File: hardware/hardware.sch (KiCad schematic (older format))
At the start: 23 parts, among them J1 6P6C, J2 RJ45_LED_Shielded, Q1 BUK7M33-60EX, U1 Teensy4.1_DEV-16771, U2 LT1910, U3 OKI, U4 OKI-78SR-3.3_1.5-W36H-C

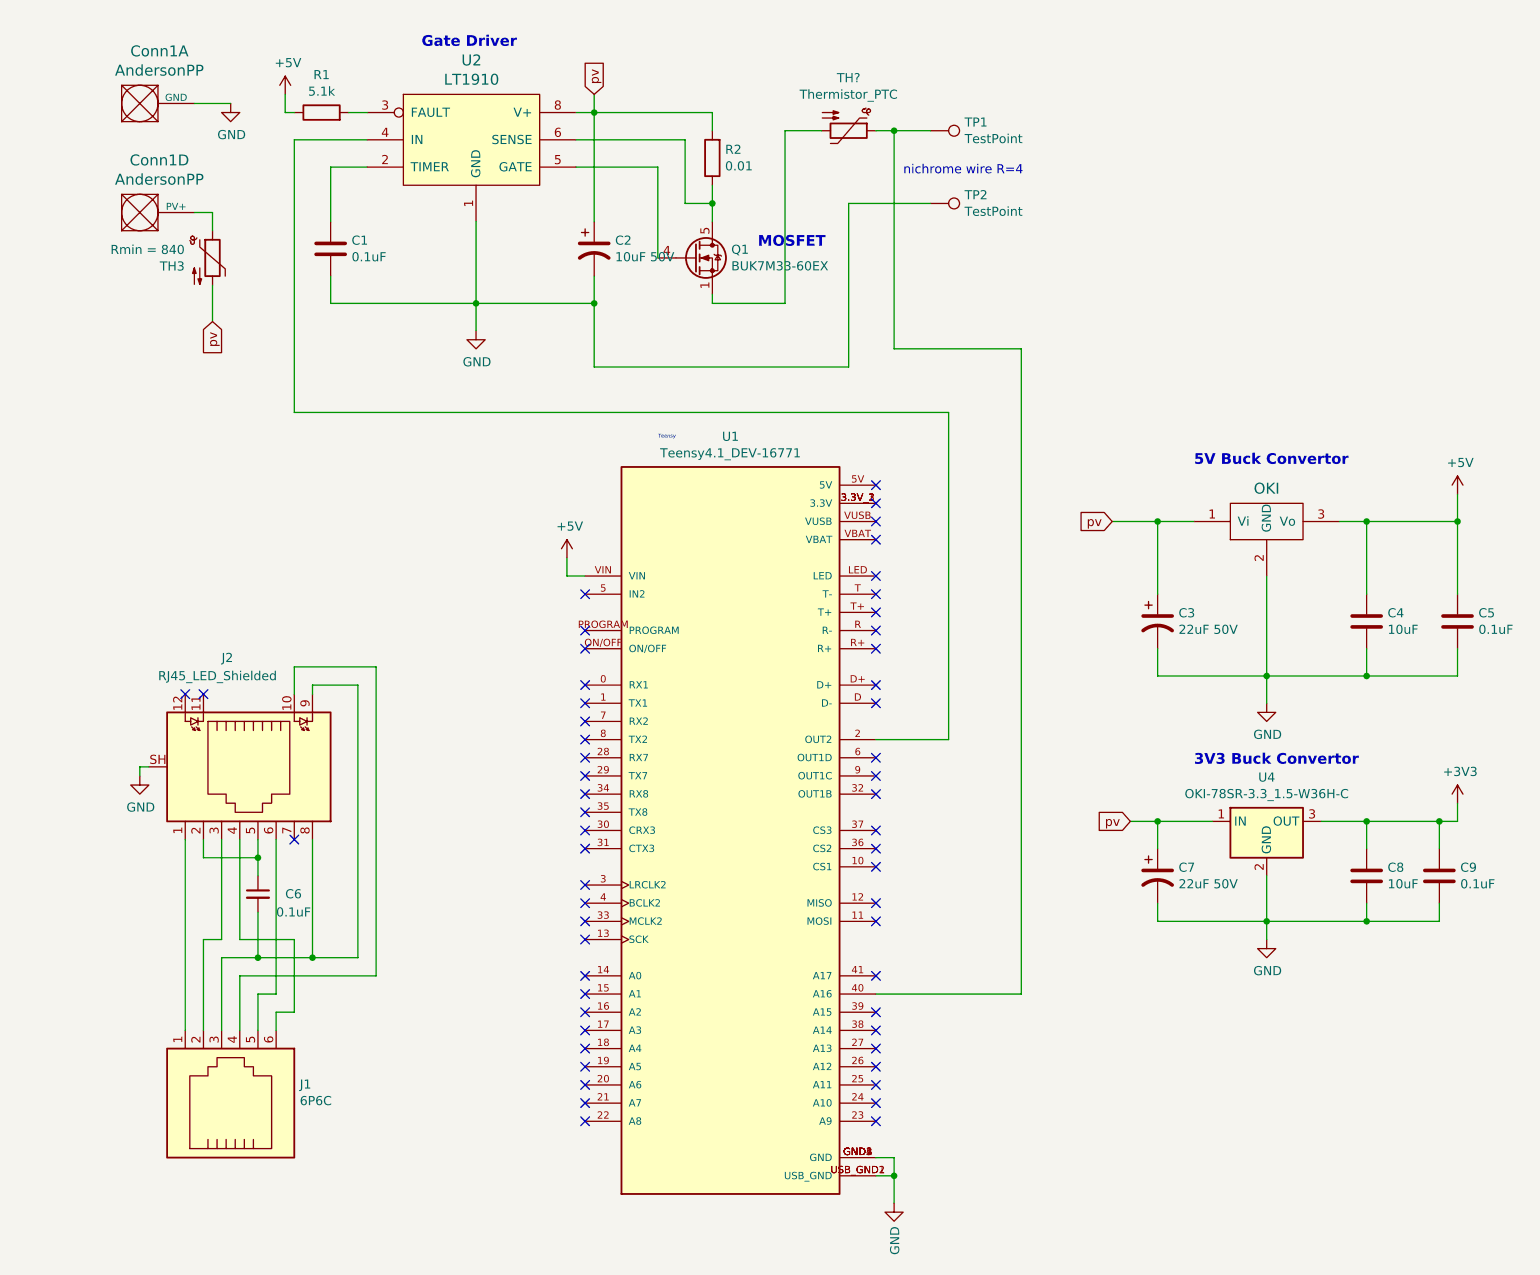
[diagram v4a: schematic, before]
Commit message: Notated and reorganized schematic
Removed measurement resistor in gate driver circuit, removed thermistor to replace with a different sensor, and wrote a note on the Andersons
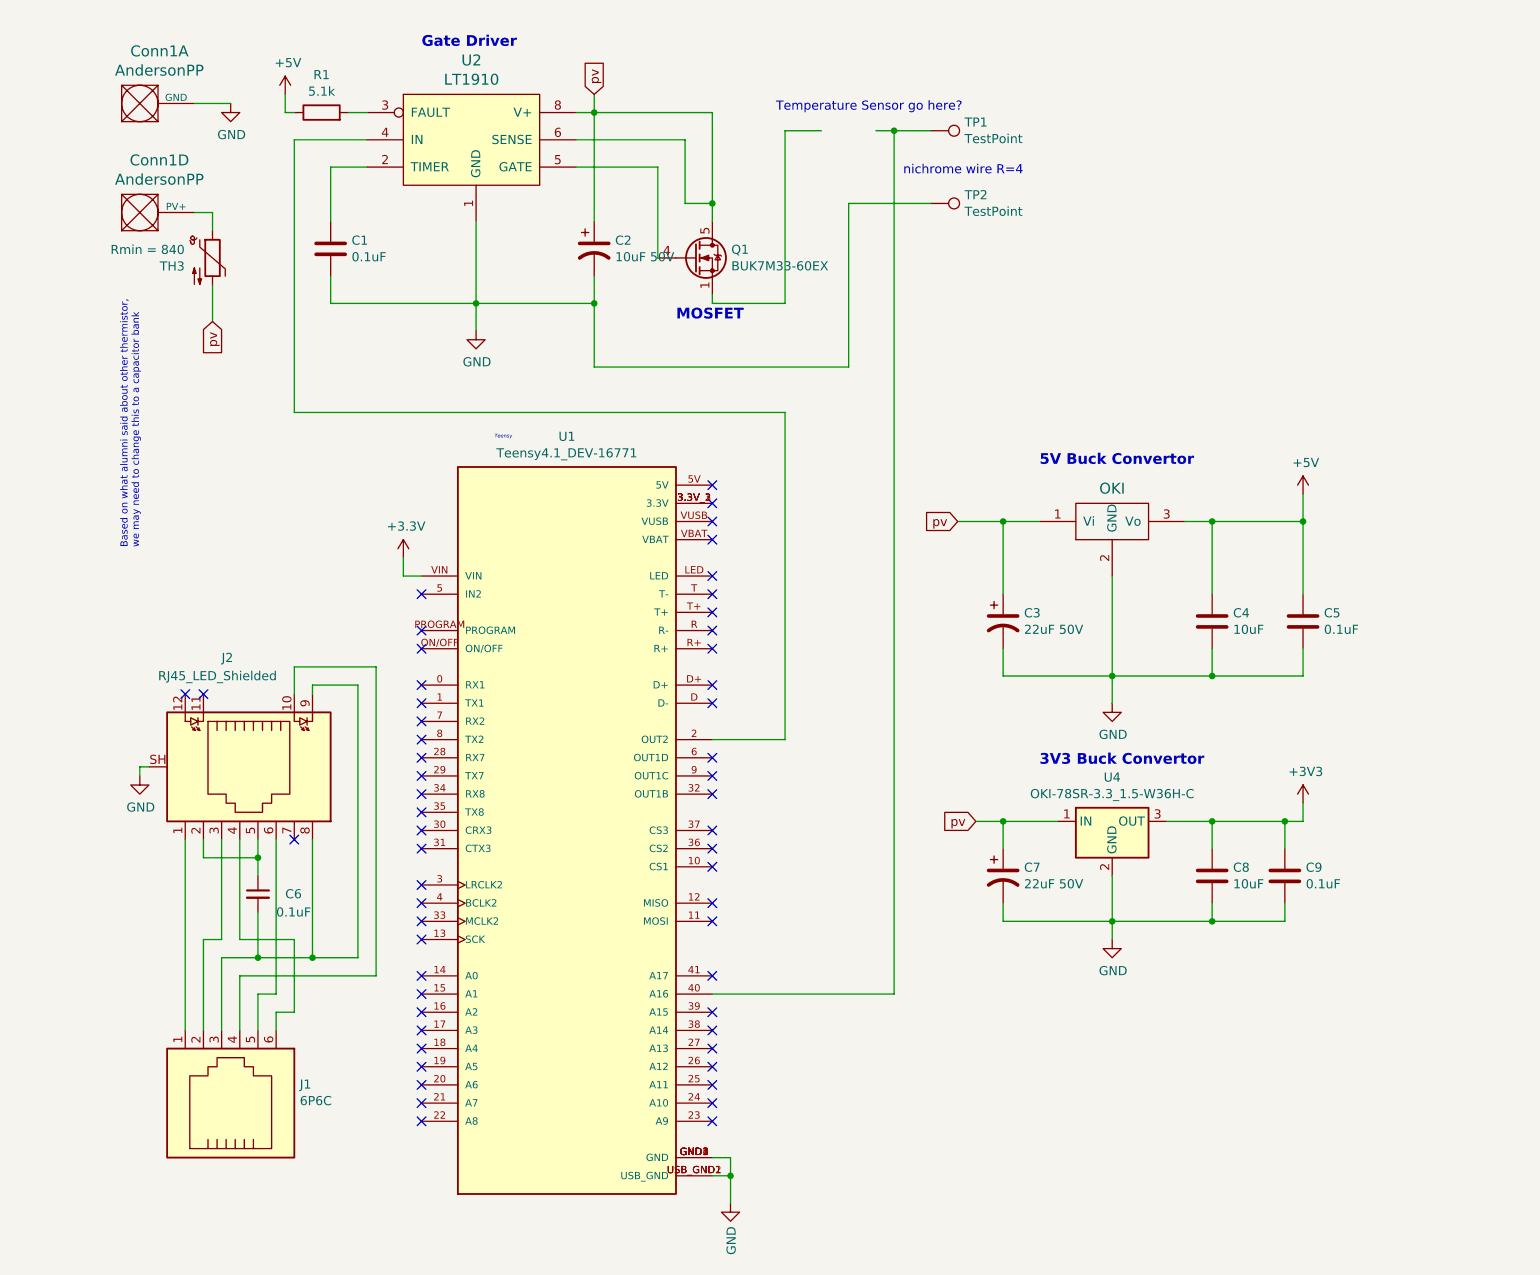
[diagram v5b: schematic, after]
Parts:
- removed R2: 0.01, symbol Device:R
- removed TH?: Thermistor_PTC, symbol Device:Thermistor_PTC
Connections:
- net +3V3: now also U1.VIN
- net +5V: no longer U1.VIN
- net pv: now also Q1.5 (D), U2.6 (SENSE)
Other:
- note added: "Based on what alumni said about other thermistor, \nwe may need to change this to a capacitor bank"
- note added: "Temperature Sensor go here?"
- moved on the sheet: C3, C4, C5, C7, C8, C9, U1, U4

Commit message: Applied footprints to capacitors
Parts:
- C1, C2, C3, C4, C5, C6, C7, C8, C9: footprint (none) -> Capacitor_SMD:C_0603_1608Metric_Pad1.08x0.95mm_HandSolder
- U1: footprint MODULE_DEV-16771 -> MRDT_Shields:MODULE_DEV-16771
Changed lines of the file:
@@
 F 0 "C1" H 1965 1746 50  0000 L CNN
 F 1 "0.1uF" H 1965 1655 50  0000 L CNN
-F 2 "" H 1888 1550 50  0001 C CNN
+F 2 "Capacitor_SMD:C_0603_1608Metric_Pad1.08x0.95mm_HandSolder" H 1888 1550 50  0001 C CNN
 F 3 "~" H 1850 1700 50  0001 C CNN
 	1    1850 1700
@@
 F 0 "C2" H 3415 1746 50  0000 L CNN
 F 1 "10uF 50V" H 3415 1655 50  0000 L CNN
-F 2 "" H 3300 1700 50  0001 C CNN
+F 2 "Capacitor_SMD:C_0603_1608Metric_Pad1.08x0.95mm_HandSolder" H 3300 1700 50  0001 C CNN
 F 3 "~" H 3300 1700 50  0001 C CNN
 	1    3300 1700
@@
 F 0 "C3" H 5665 3796 50  0000 L CNN
 F 1 "22uF 50V" H 5665 3705 50  0000 L CNN
-F 2 "" H 5550 3750 50  0001 C CNN
+F 2 "Capacitor_SMD:C_0603_1608Metric_Pad1.08x0.95mm_HandSolder" H 5550 3750 50  0001 C CNN
 F 3 "~" H 5550 3750 50  0001 C CNN
 	1    5550 3750
@@
 F 0 "C4" H 6815 3796 50  0000 L CNN
 F 1 "10uF" H 6815 3705 50  0000 L CNN
-F 2 "" H 6738 3600 50  0001 C CNN
+F 2 "Capacitor_SMD:C_0603_1608Metric_Pad1.08x0.95mm_HandSolder" H 6738 3600 50  0001 C CNN
 F 3 "~" H 6700 3750 50  0001 C CNN
 	1    6700 3750
@@
 F 0 "C5" H 7315 3796 50  0000 L CNN
 F 1 "0.1uF" H 7315 3705 50  0000 L CNN
-F 2 "" H 7238 3600 50  0001 C CNN
+F 2 "Capacitor_SMD:C_0603_1608Metric_Pad1.08x0.95mm_HandSolder" H 7238 3600 50  0001 C CNN
 F 3 "~" H 7200 3750 50  0001 C CNN
 	1    7200 3750
@@
 F 0 "C7" H 5665 5196 50  0000 L CNN
 F 1 "22uF 50V" H 5665 5105 50  0000 L CNN
-F 2 "" H 5550 5150 50  0001 C CNN
+F 2 "Capacitor_SMD:C_0603_1608Metric_Pad1.08x0.95mm_HandSolder" H 5550 5150 50  0001 C CNN
 F 3 "~" H 5550 5150 50  0001 C CNN
 	1    5550 5150
@@
 F 0 "C8" H 6815 5196 50  0000 L CNN
 F 1 "10uF" H 6815 5105 50  0000 L CNN
-F 2 "" H 6738 5000 50  0001 C CNN
+F 2 "Capacitor_SMD:C_0603_1608Metric_Pad1.08x0.95mm_HandSolder" H 6738 5000 50  0001 C CNN
 F 3 "~" H 6700 5150 50  0001 C CNN
 	1    6700 5150
@@
 F 0 "C9" H 7215 5196 50  0000 L CNN
 F 1 "0.1uF" H 7215 5105 50  0000 L CNN
-F 2 "" H 7138 5000 50  0001 C CNN
+F 2 "Capacitor_SMD:C_0603_1608Metric_Pad1.08x0.95mm_HandSolder" H 7138 5000 50  0001 C CNN
 F 3 "~" H 7100 5150 50  0001 C CNN
 	1    7100 5150
@@
 F 0 "U1" H 3150 7067 50  0000 C CNN
 F 1 "Teensy4.1_DEV-16771" H 3150 6976 50  0000 C CNN
-F 2 "MODULE_DEV-16771" H 5250 4600 50  0001 L BNN
+F 2 "MRDT_Shields:MODULE_DEV-16771" H 5250 4600 50  0001 L BNN
 F 3 "" H 3150 4900 50  0001 L BNN
 F 4 "Manufacturer recommendations" H 5250 4350 50  0001 L BNN "STANDARD"
@@
 F 0 "C6" H 1600 5250 50  0000 L CNN
 F 1 "0.1uF" H 1550 5150 50  0000 L CNN
-F 2 "" H 1450 5250 50  0001 C CNN
+F 2 "Capacitor_SMD:C_0603_1608Metric_Pad1.08x0.95mm_HandSolder" H 1450 5250 50  0001 C CNN
 F 3 "~" H 1450 5250 50  0001 C CNN
 	1    1450 5250
@@
 	3950 5800 4950 5800
 $Comp
-L power:+3.3V #PWR?
+L power:+3.3V #PWR0101
 U 1 1 617FDF47
 P 2250 3400
-F 0 "#PWR?" H 2250 3250 50  0001 C CNN
+F 0 "#PWR0101" H 2250 3250 50  0001 C CNN
 F 1 "+3.3V" H 2265 3573 50  0000 C CNN
 F 2 "" H 2250 3400 50  0001 C CNN

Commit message: Assigned footprints and started layout
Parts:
- Conn1: footprint (none) -> MRDT_Connectors:Anderson_1_Horizontal
- R1: footprint (none) -> Resistor_SMD:R_0603_1608Metric_Pad0.98x0.95mm_HandSolder
- U2: footprint (none) -> Package_SO:SOIC-8-N7_3.9x4.9mm_P1.27mm
- U3: footprint (none) -> MRDT_Devices:OKI_Horizontal
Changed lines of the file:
@@
 F 0 "Conn1" H 908 1987 60  0000 C CNN
 F 1 "AndersonPP" H 908 1881 60  0000 C CNN
-F 2 "" H 550 1050 60  0001 C CNN
+F 2 "MRDT_Connectors:Anderson_1_Horizontal" H 550 1050 60  0001 C CNN
 F 3 "" H 550 1050 60  0001 C CNN
 	4    700  1600
@@
 F 0 "Conn1" H 908 1387 60  0000 C CNN
 F 1 "AndersonPP" H 908 1281 60  0000 C CNN
-F 2 "" H 550 450 60  0001 C CNN
+F 2 "MRDT_Connectors:Anderson_1_Horizontal" H 550 450 60  0001 C CNN
 F 3 "" H 550 450 60  0001 C CNN
 	1    700  1000
@@
 F 0 "U2" H 2625 2037 60  0000 C CNN
 F 1 "LT1910" H 2625 1931 60  0000 C CNN
-F 2 "" H 2250 1350 60  0001 C CNN
+F 2 "Package_SO:SOIC-8-N7_3.9x4.9mm_P1.27mm" H 2250 1350 60  0001 C CNN
 F 3 "" H 2250 1350 60  0001 C CNN
 	1    2250 1350
@@
 F 0 "R1" V 2007 950 50  0000 C CNN
 F 1 "5.1k" V 1916 950 50  0000 C CNN
-F 2 "" V 1730 950 50  0001 C CNN
+F 2 "Resistor_SMD:R_0603_1608Metric_Pad0.98x0.95mm_HandSolder" V 1730 950 50  0001 C CNN
 F 3 "~" H 1800 950 50  0001 C CNN
 	1    1800 950
@@
 F 0 "U3" H 6000 3250 60  0001 C CNN
 F 1 "OKI" H 6150 3581 60  0000 C CNN
-F 2 "" H 5750 3200 60  0001 C CNN
+F 2 "MRDT_Devices:OKI_Horizontal" H 5750 3200 60  0001 C CNN
 F 3 "" H 5750 3200 60  0001 C CNN
 	1    5950 3300

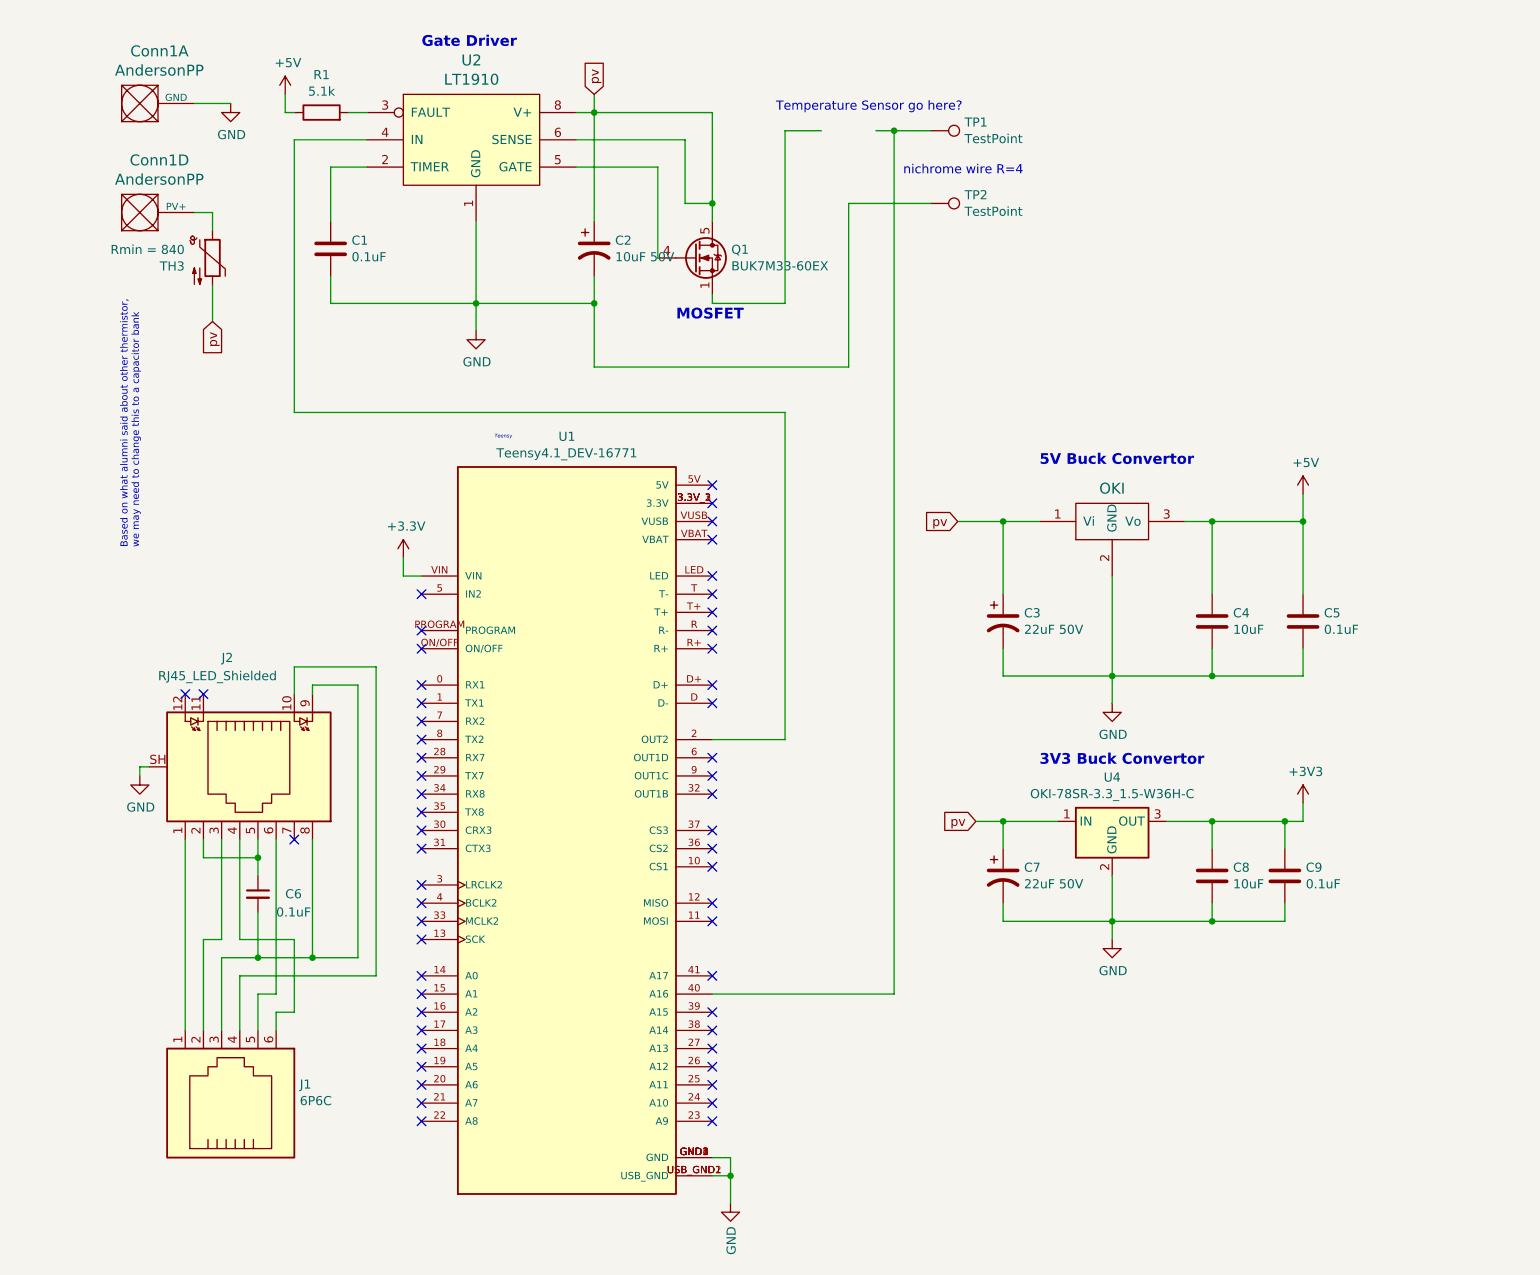
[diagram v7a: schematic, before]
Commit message: Changed PV to 12V and added TH OpAmp circuit
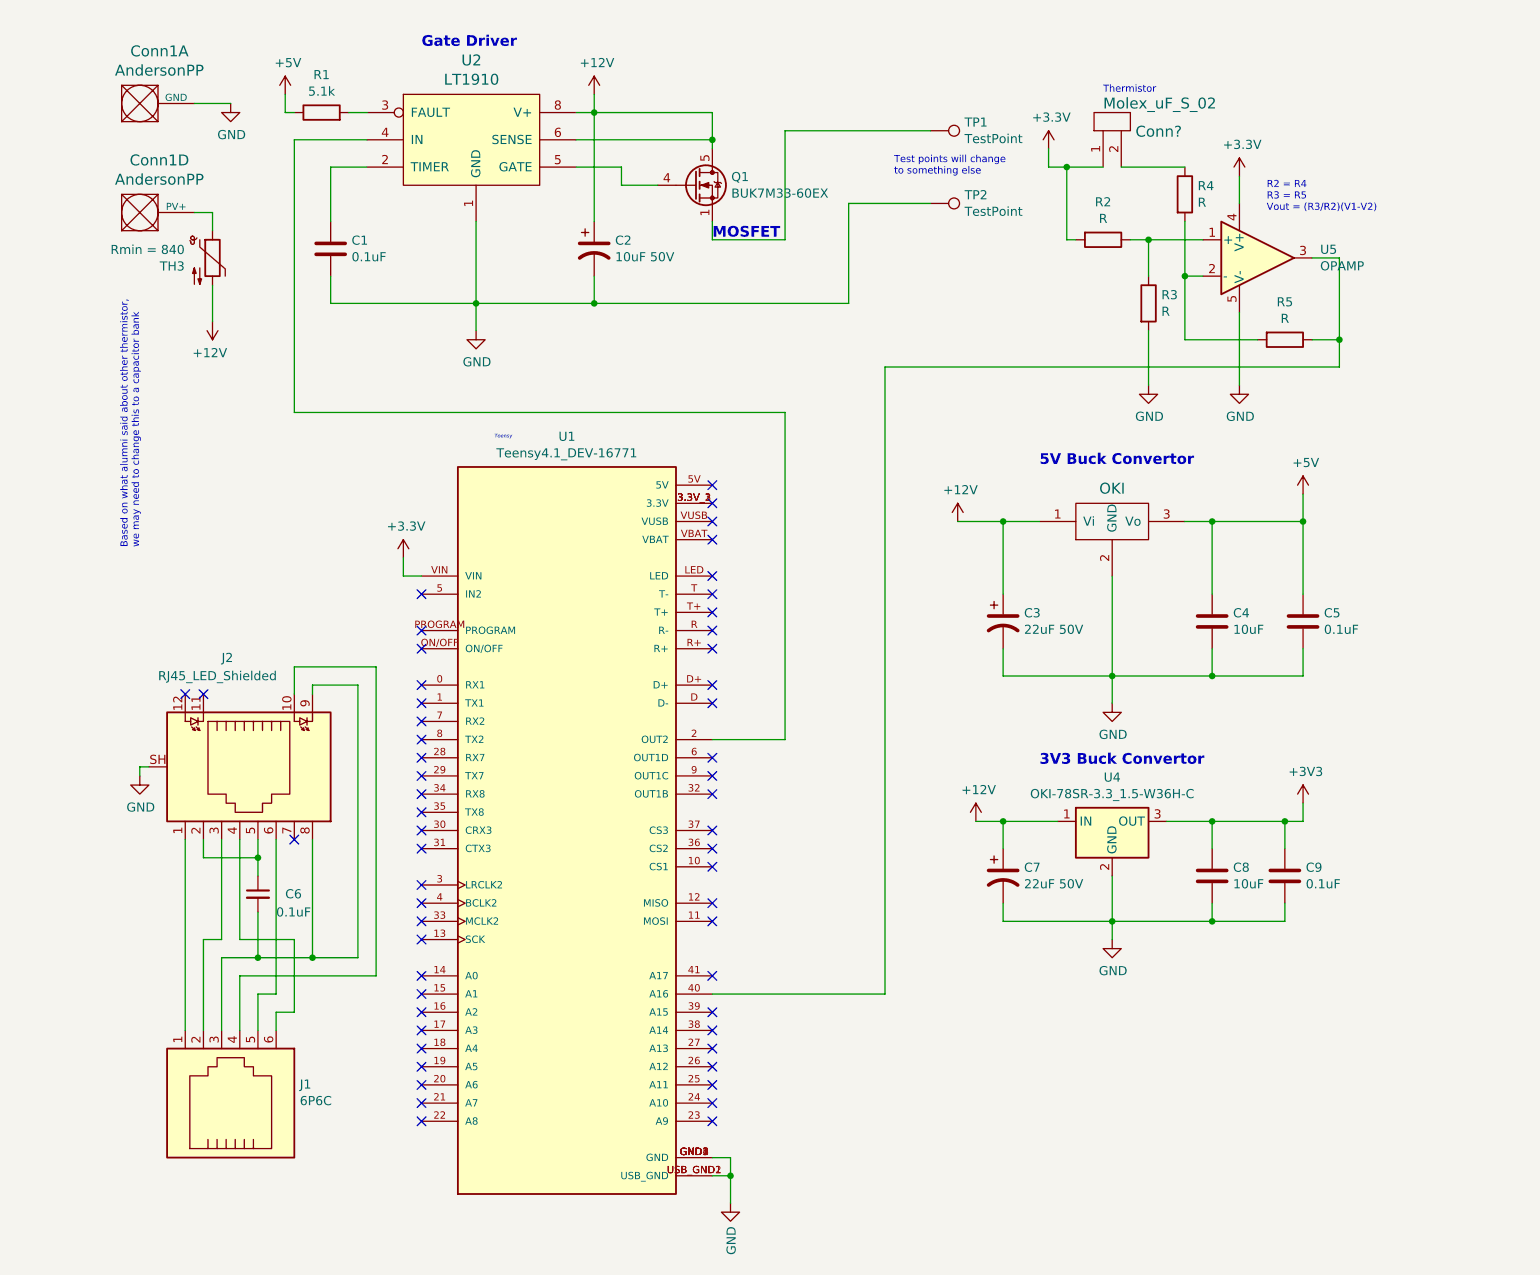
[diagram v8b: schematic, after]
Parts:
- added Conn?: Molex_uF_S_02, MRDT_Connectors:MOLEX_uF_S_02_Horizontal, symbol MRDT_Connectors:Molex_uF_S_02
- added R2, R3, R4, R5: R, symbol Device:R
- added U5: OPAMP, symbol pspice:OPAMP
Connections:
- net +3V3: now also Conn?.1, R2.2, U5.4 (V+)
- net GND: now also R3.2, U5.5 (V-)
- net at U1.40 (A16): now also R5.1, U5.3; no longer TP1.1
- net at Q1.1 (S), Q1.2 (S), Q1.3 (S): now also TP1.1
- net pv renamed +12V
- new net: R2.1, R3.1, U5.1 (+)
- new net: R4.2, R5.2, U5.2 (-)
- new net: Conn?.2, R4.1
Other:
- note added: "R2 = R4\nR3 = R5\nVout = (R3/R2)(V1-V2)"
- note added: "Test points will change\nto something else"
- note added: "Thermistor"
- note removed: "Temperature Sensor go here?"
- note removed: "nichrome wire R=4"
- moved on the sheet: Q1
